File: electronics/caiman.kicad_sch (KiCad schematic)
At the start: 125 parts, among them J1 Conn_01x03_Pin, J10 Conn_01x04_Pin, J11 Conn_01x04_Pin, J12 Conn_01x04_Pin, J13 Micro_SD_Card, J14 50 ohm, J15 Conn_01x03_Pin, J2 Conn_01x04_Pin, J3 Conn_01x04_Pin, J4 Conn_01x03_Pin, J5 Conn_01x04_Pin, J6 Conn_01x04_Pin, J7 Conn_01x02_Pin, J8 Conn_01x02_Pin, J9 Conn_01x02_Pin, Q1 Q_PMOS-E_Generic_SSSGD, Q2 AON6262E, U1 AP63205WU, U10 SN74LV1T34DBV, U2 AP63203WU, U3 US1881, U4 LM74700, U5 LPS22HBTR, U6 LIS2MDLTR, U7 STM32F765VITx, U8 LSM6DSO, U9 nRF24L01P, Y1 25MHz, Y2 16MHz

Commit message: Updating the PCB
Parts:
- added JP1: SolderJumper_2_Open, Jumper:SolderJumper-2_P1.3mm_Open_TrianglePad1.0x1.5mm, symbol Jumper:SolderJumper_2_Open
- added R12: 10k, Resistor_SMD:R_0402_1005Metric, symbol Device:R
- C10, C9: value 0.1uF -> 0.1uF, 50V; footprint Capacitor_SMD:C_0603_1608Metric -> Capacitor_SMD:C_0805_2012Metric
- C11: value 47uF -> 47uF, 50v
- C3: value 10uF -> 10uF, 50v; footprint Capacitor_SMD:C_0603_1608Metric -> Capacitor_SMD:C_0805_2012Metric
- C4, C5, C7, C8: value 22uF -> 22uF, 16V
- C6: value 10uF -> 10uF, 16v; footprint Capacitor_SMD:C_0603_1608Metric -> Capacitor_SMD:C_0805_2012Metric
- L1: value 3.3uH -> 4.7uH
- L2: value 2.2uH -> 3.9uH
- R7: value 27k -> 10k
- Y1: value 25MHz -> 8MHz
- renumbered R12 to R13, R13 to R14, R14 to R15, R15 to R16, R16 to R17, R17 to R18, R18 to R19, R19 to R20, R20 to R21, R21 to R22, R22 to R23, R23 to R24, R24 to R25, R25 to R26, R26 to R27, R27 to R28, R28 to R29, R29 to R30, R30 to R31, R31 to R32
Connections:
- net +3V3: now also JP1.1 (A)
- net GND: now also R12.2
- net VCC: now also R1.1; no longer R1.2, R2.1
- net at U7.94 (BOOT0): now also JP1.2 (B), R12.1
- net at U1.2 (EN): now also R1.2, R2.1; no longer R1.1
- no-connect marks 51 -> 50
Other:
- moved on the sheet: R1, R2

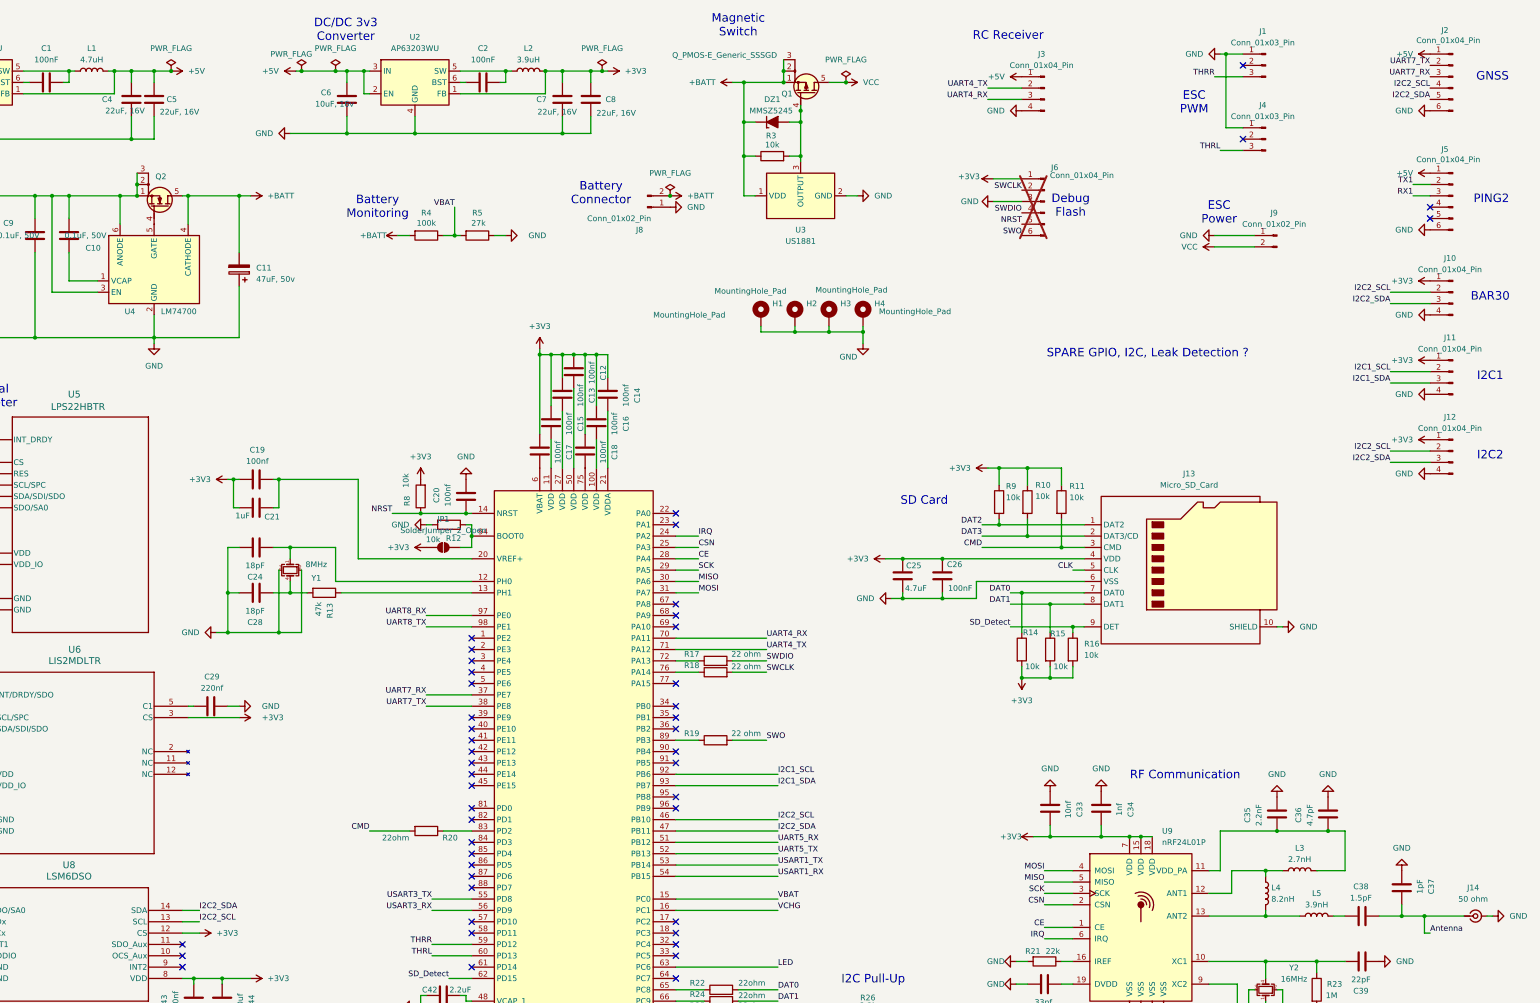
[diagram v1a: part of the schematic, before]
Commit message: STM32 Power Supply correction
Modified series capacitors to parallel capacitors in STM32
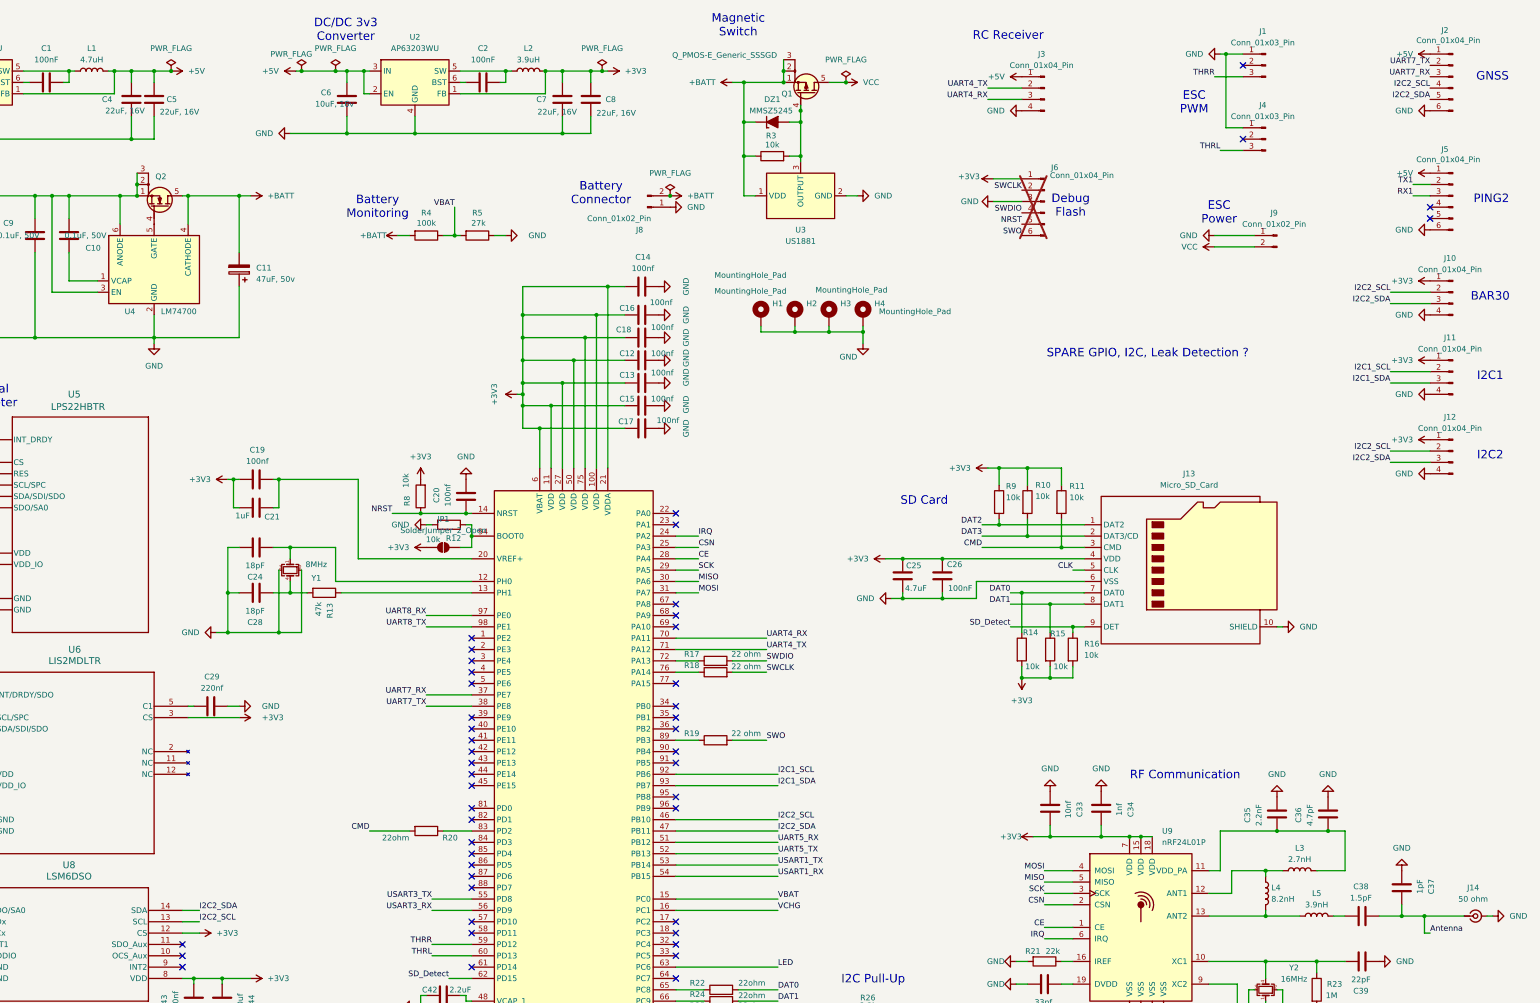
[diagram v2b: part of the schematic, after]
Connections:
- net +3V3: now also U7.100 (VDD), U7.11 (VDD), U7.21 (VDDA), U7.27 (VDD), U7.50 (VDD), U7.6 (VBAT), U7.75 (VDD)
- net GND: now also C12.1, C13.1, C14.1, C15.1, C16.1, C17.1, C18.1
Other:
- moved on the sheet: C12, C13, C14, C15, C16, C17, C18
